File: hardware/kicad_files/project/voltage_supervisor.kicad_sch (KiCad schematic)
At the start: 2 parts, among them U8 MCP1319MT-29LE-OT

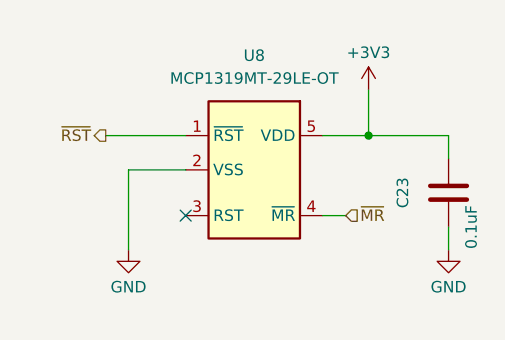
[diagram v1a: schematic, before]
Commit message: fix: replace all local symbols and footprints with versions from KiCad or project libraries
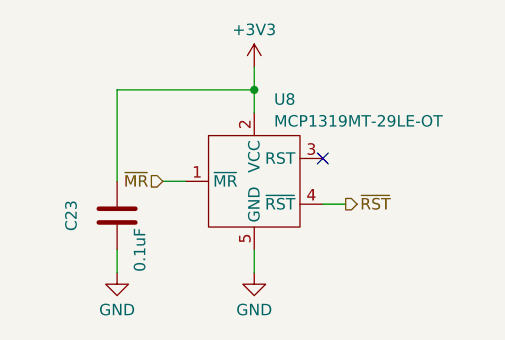
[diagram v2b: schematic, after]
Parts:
- U8: footprint Caravel_Board:PoR_5_SOT23 -> Package_TO_SOT_SMD:SOT-23-5; symbol Caravel_board:MCP1319MT-29LE-OT -> custom_symbols:MCP1319MT-29LE-OT
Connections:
- net +3V3: now also U8.2 (VCC); no longer U8.5 (VDD)
- net GND: now also U8.5 (GND); no longer U8.2 (VSS)
- net ~{MR}: now also U8.1 (~{MR}); no longer U8.4 (~{MR})
- net ~{RST}: now also U8.4 (~{RST}); no longer U8.1 (~{RST})
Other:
- moved on the sheet: C23
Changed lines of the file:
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@@
 	)
 	(junction
-		(at 139.7 95.25)
+		(at 127 90.17)
 		(diameter 0)
 		(color 0 0 0 0)
 	)
 	(no_connect
-		(at 119.38 104.14)
-	)
-	(wire
-		(pts
-			(xy 148.59 95.25) (xy 148.59 97.79)
-		)
-		(stroke
-			(width 0)
-			(type default)
-		)
-	)
-	(wire
-		(pts
-			(xy 134.62 95.25) (xy 139.7 95.25)
-		)
-		(stroke
-			(width 0)
-			(type default)
-		)
-	)
-	(wire
-		(pts
-			(xy 148.59 105.41) (xy 148.59 107.95)
-		)
-		(stroke
-			(width 0)
-			(type default)
-		)
-	)
-	(wire
-		(pts
-			(xy 139.7 95.25) (xy 148.59 95.25)
-		)
-		(stroke
-			(width 0)
-			(type default)
-		)
-	)
-	(wire
-		(pts
-			(xy 137.16 104.14) (xy 134.62 104.14)
-		)
-		(stroke
-			(width 0)
-			(type default)
-		)
-	)
-	(wire
-		(pts
-			(xy 113.03 107.95) (xy 113.03 99.06)
-		)
-		(stroke
-			(width 0)
-			(type default)
-		)
-	)
-	(wire
-		(pts
-			(xy 110.49 95.25) (xy 119.38 95.25)
-		)
-		(stroke
-			(width 0)
-			(type default)
-		)
-	)
-	(wire
-		(pts
-			(xy 113.03 99.06) (xy 119.38 99.06)
-		)
-		(stroke
-			(width 0)
-			(type default)
-		)
-	)
-	(wire
-		(pts
-			(xy 139.7 95.25) (xy 139.7 90.17)
+		(at 134.62 97.79)
+	)
+	(wire
+		(pts
+			(xy 127 90.17) (xy 127 92.71)
+		)
+		(stroke
+			(width 0)
+			(type default)
+		)
+	)
+	(wire
+		(pts
+			(xy 127 90.17) (xy 127 87.63)
+		)
+		(stroke
+			(width 0)
+			(type default)
+		)
+	)
+	(wire
+		(pts
+			(xy 111.76 90.17) (xy 111.76 100.33)
+		)
+		(stroke
+			(width 0)
+			(type default)
+		)
+	)
+	(wire
+		(pts
+			(xy 137.16 102.87) (xy 134.62 102.87)
+		)
+		(stroke
+			(width 0)
+			(type default)
+		)
+	)
+	(wire
+		(pts
+			(xy 111.76 107.95) (xy 111.76 110.49)
+		)
+		(stroke
+			(width 0)
+			(type default)
+		)
+	)
+	(wire
+		(pts
+			(xy 111.76 90.17) (xy 127 90.17)
+		)
+		(stroke
+			(width 0)
+			(type default)
+		)
+	)
+	(wire
+		(pts
+			(xy 116.84 100.33) (xy 119.38 100.33)
+		)
+		(stroke
+			(width 0)
+			(type default)
+		)
+	)
+	(wire
+		(pts
+			(xy 127 110.49) (xy 127 107.95)
 		)
 		(stroke
@@
 	(hierarchical_label "~{RST}"
 		(shape output)
-		(at 110.49 95.25 180)
+		(at 137.16 102.87 0)
 		(fields_autoplaced yes)
 		(effects
@@
 				(size 1.27 1.27)
 			)
-			(justify right)
+			(justify left)
 		)
 	)
 	(hierarchical_label "~{MR}"
 		(shape input)
-		(at 137.16 104.14 0)
+		(at 116.84 100.33 180)
 		(fields_autoplaced yes)
 		(effects
@@
 				(size 1.27 1.27)
 			)
-			(justify left)
+			(justify right)
 		)
 	)
 	(symbol
 		(lib_id "power:+3V3")
-		(at 139.7 90.17 0)
+		(at 127 87.63 0)
 		(unit 1)
 		(exclude_from_sim no)
@@
 		(dnp no)
 		(fields_autoplaced yes)
-		(property "Reference" "#PWR059"
-			(at 139.7 93.98 0)
+		(property "Reference" "#PWR066"
+			(at 127 91.44 0)
 			(effects
 				(font
@@
 		)
 		(property "Value" "+3V3"
-			(at 139.7 86.0369 0)
+			(at 127 83.4969 0)
 			(effects
 				(font
@@
 		)
 		(property "Footprint" ""
-			(at 139.7 90.17 0)
+			(at 127 87.63 0)
 			(effects
 				(font
@@
 		)
 		(property "Datasheet" ""
-			(at 139.7 90.17 0)
+			(at 127 87.63 0)
 			(effects
 				(font
@@
 		)
 		(property "Description" "Power symbol creates a global label with name \"+3V3\""
-			(at 139.7 90.17 0)
+			(at 127 87.63 0)
 			(effects
 				(font
@@
 			(project "FABulous_board"
 				(path "/5664f05e-a3ef-4177-8026-c4580fa32c71/61abf8ce-9ba2-4995-9a57-37e178bb3e97"
-					(reference "#PWR059")
+					(reference "#PWR066")
 					(unit 1)
 				)
@@
 	(symbol
 		(lib_id "Device:C")
-		(at 148.59 101.6 180)
+		(at 111.76 104.14 180)
 		(unit 1)
 		(exclude_from_sim no)
@@
 		(dnp no)
 		(property "Reference" "C23"
-			(at 143.51 101.6 90)
+			(at 106.68 104.14 90)
 			(effects
 				(font
@@
 		)
 		(property "Value" "0.1uF"
-			(at 151.13 105.41 90)
+			(at 114.3 107.95 90)
 			(effects
 				(font
@@
 		)
 		(property "Footprint" "Capacitor_SMD:C_0805_2012Metric"
-			(at 147.6248 97.79 0)
+			(at 110.7948 100.33 0)
 			(effects
 				(font
@@
 		)
 		(property "Datasheet" "~"
-			(at 148.59 101.6 0)
+			(at 111.76 104.14 0)
 			(effects
 				(font
@@
 		)
 		(property "Description" "Unpolarized capacitor"
-			(at 148.59 101.6 0)
+			(at 111.76 104.14 0)
 			(effects
 				(font
@@
 	)
 	(symbol
-		(lib_id "Caravel_board:MCP1319MT-29LE-OT")
+		(lib_id "custom_symbols:MCP1319MT-29LE-OT")
 		(at 127 99.06 0)
 		(unit 1)
@@
 		(fields_autoplaced yes)
 		(property "Reference" "U8"
-			(at 127 86.36 0)
-			(effects
-				(font
-					(size 1.27 1.27)
-				)
+			(at 129.1941 91.2325 0)
+			(effects
+				(font
+					(size 1.27 1.27)
+				)
+				(justify left)
 			)
 		)
 		(property "Value" "MCP1319MT-29LE-OT"
-			(at 127 88.9 0)
-			(effects
-				(font
-					(size 1.27 1.27)
-				)
-			)
-		)
-		(property "Footprint" "Caravel_Board:PoR_5_SOT23"
-			(at 147.32 107.95 0)
+			(at 129.1941 93.6568 0)
+			(effects
+				(font
+					(size 1.27 1.27)
+				)
+				(justify left)
+			)
+		)
+		(property "Footprint" "Package_TO_SOT_SMD:SOT-23-5"
+			(at 127 99.06 0)
 			(effects
 				(font
@@
 	(symbol
 		(lib_id "power:GND")
-		(at 113.03 107.95 0)
+		(at 127 110.49 0)
 		(unit 1)
 		(exclude_from_sim no)
@@
 		(dnp no)
 		(fields_autoplaced yes)
-		(property "Reference" "#PWR058"
-			(at 113.03 114.3 0)
+		(property "Reference" "#PWR067"
+			(at 127 116.84 0)
 			(effects
 				(font
@@
 		)
 		(property "Value" "GND"
-			(at 113.03 112.0831 0)
+			(at 127 114.6231 0)
 			(effects
 				(font
@@
 		)
 		(property "Footprint" ""
-			(at 113.03 107.95 0)
+			(at 127 110.49 0)
 			(effects
 				(font
@@
 		)
 		(property "Datasheet" ""
-			(at 113.03 107.95 0)
+			(at 127 110.49 0)
 			(effects
 				(font
@@
 		)
 		(property "Description" "Power symbol creates a global label with name \"GND\" , ground"
-			(at 113.03 107.95 0)
+			(at 127 110.49 0)
 			(effects
 				(font
@@
 			(project "FABulous_board"
 				(path "/5664f05e-a3ef-4177-8026-c4580fa32c71/61abf8ce-9ba2-4995-9a57-37e178bb3e97"
-					(reference "#PWR058")
+					(reference "#PWR067")
 					(unit 1)
 				)
@@
 	(symbol
 		(lib_id "power:GND")
-		(at 148.59 107.95 0)
+		(at 111.76 110.49 0)
 		(unit 1)
 		(exclude_from_sim no)
@@
 		(dnp no)
 		(fields_autoplaced yes)
-		(property "Reference" "#PWR060"
-			(at 148.59 114.3 0)
+		(property "Reference" "#PWR065"
+			(at 111.76 116.84 0)
 			(effects
 				(font
@@
 		)
 		(property "Value" "GND"
-			(at 148.59 112.0831 0)
+			(at 111.76 114.6231 0)
 			(effects
 				(font
@@
 		)
 		(property "Footprint" ""
-			(at 148.59 107.95 0)
+			(at 111.76 110.49 0)
 			(effects
 				(font
@@
 		)
 		(property "Datasheet" ""
-			(at 148.59 107.95 0)
+			(at 111.76 110.49 0)
 			(effects
 				(font
@@
 		)
 		(property "Description" "Power symbol creates a global label with name \"GND\" , ground"
-			(at 148.59 107.95 0)
+			(at 111.76 110.49 0)
 			(effects
 				(font
@@
 			(project "FABulous_board"
 				(path "/5664f05e-a3ef-4177-8026-c4580fa32c71/61abf8ce-9ba2-4995-9a57-37e178bb3e97"
-					(reference "#PWR060")
+					(reference "#PWR065")
 					(unit 1)
 				)
